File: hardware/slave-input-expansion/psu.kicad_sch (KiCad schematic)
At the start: 15 parts

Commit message: Diseño mecanico del ensamblaje
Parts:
- C4, C5: value (none) -> 100nF; footprint (none) -> Capacitor_SMD:C_1206_3216Metric_Pad1.33x1.80mm_HandSolder
- C6, C7: value (none) -> 470uF; footprint (none) -> libs:CAP_10x10_SMD_THT
- D2: value (none) -> LED; footprint (none) -> LED_SMD:LED_1206_3216Metric
- D3, D4: value (none) -> SS14; footprint (none) -> Diode_SMD:D_SMA_Handsoldering
- L1, L2: value (none) -> 68uH; footprint (none) -> libs:L_12x12mm_H8mm
- R25: value (none) -> 4K7; footprint (none) -> Resistor_SMD:R_1206_3216Metric
- R26: value (none) -> 5.6K; footprint (none) -> Resistor_THT:R_Axial_DIN0204_L3.6mm_D1.6mm_P2.54mm_Vertical
- R27: value (none) -> 12K; footprint (none) -> Resistor_THT:R_Axial_DIN0204_L3.6mm_D1.6mm_P2.54mm_Vertical
- U12, U13: value (none) -> LM2596S-3.3; footprint (none) -> libs:TO-263-5_TabPin3
- U14: value (none) -> AMS1117-5.0; footprint (none) -> Package_TO_SOT_SMD:SOT-223-3_TabPin2
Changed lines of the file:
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@@
     (in_bom yes) (on_board yes)
     (property "Reference" "U13" (id 0) (at 107.95 80.01 0))
-    (property "Value" "" (id 1) (at 120.65 80.01 0))
-    (property "Footprint" "" (id 2) (at 118.11 92.71 0)
+    (property "Value" "LM2596S-3.3" (id 1) (at 120.65 80.01 0))
+    (property "Footprint" "libs:TO-263-5_TabPin3" (id 2) (at 118.11 92.71 0)
       (effects (font (size 1.27 1.27) italic) (justify left) hide)
     )
@@
       (effects (font (size 1.27 1.27)) (justify right))
     )
-    (property "Value" "" (id 1) (at 57.6072 90.2208 90)
+    (property "Value" "LED" (id 1) (at 57.6072 90.2208 90)
       (effects (font (size 1.27 1.27)) (justify right))
     )
-    (property "Footprint" "" (id 2) (at 54.61 88.9 0)
+    (property "Footprint" "LED_SMD:LED_1206_3216Metric" (id 2) (at 54.61 88.9 0)
       (effects (font (size 1.27 1.27)) hide)
     )
@@
       (effects (font (size 1.27 1.27)) (justify left))
     )
-    (property "Value" "" (id 1) (at 56.388 100.203 0)
-      (effects (font (size 1.27 1.27)) (justify left))
-    )
-    (property "Footprint" "" (id 2) (at 52.832 99.06 90)
+    (property "Value" "4K7" (id 1) (at 56.388 100.203 0)
+      (effects (font (size 1.27 1.27)) (justify left))
+    )
+    (property "Footprint" "Resistor_SMD:R_1206_3216Metric" (id 2) (at 52.832 99.06 90)
       (effects (font (size 1.27 1.27)) hide)
     )
@@
       (effects (font (size 1.27 1.27)) (justify left))
     )
-    (property "Value" "" (id 1) (at 95.25 97.79 0)
-      (effects (font (size 1.27 1.27)) (justify left))
-    )
-    (property "Footprint" "" (id 2) (at 94.9452 99.06 0)
+    (property "Value" "100nF" (id 1) (at 95.25 97.79 0)
+      (effects (font (size 1.27 1.27)) (justify left))
+    )
+    (property "Footprint" "Capacitor_SMD:C_1206_3216Metric_Pad1.33x1.80mm_HandSolder" (id 2) (at 94.9452 99.06 0)
       (effects (font (size 1.27 1.27)) hide)
     )
@@
       (effects (font (size 1.27 1.27)) (justify left))
     )
-    (property "Value" "" (id 1) (at 134.112 96.393 90)
-      (effects (font (size 1.27 1.27)) (justify left))
-    )
-    (property "Footprint" "" (id 2) (at 127.635 95.25 0)
+    (property "Value" "SS14" (id 1) (at 134.112 96.393 90)
+      (effects (font (size 1.27 1.27)) (justify left))
+    )
+    (property "Footprint" "Diode_SMD:D_SMA_Handsoldering" (id 2) (at 127.635 95.25 0)
       (effects (font (size 1.27 1.27)) hide)
     )
@@
       (effects (font (size 1.27 1.27)) (justify left))
     )
-    (property "Value" "" (id 1) (at 182.0672 95.25 0)
-      (effects (font (size 1.27 1.27)) (justify left))
-    )
-    (property "Footprint" "" (id 2) (at 180.0352 99.06 0)
+    (property "Value" "470uF" (id 1) (at 182.0672 95.25 0)
+      (effects (font (size 1.27 1.27)) (justify left))
+    )
+    (property "Footprint" "libs:CAP_10x10_SMD_THT" (id 2) (at 180.0352 99.06 0)
       (effects (font (size 1.27 1.27)) hide)
     )
@@
     (in_bom yes) (on_board yes)
     (property "Reference" "L2" (id 0) (at 147.32 90.17 90))
-    (property "Value" "" (id 1) (at 152.4 90.17 90))
-    (property "Footprint" "" (id 2) (at 149.86 88.9 0)
+    (property "Value" "68uH" (id 1) (at 152.4 90.17 90))
+    (property "Footprint" "libs:L_12x12mm_H8mm" (id 2) (at 149.86 88.9 0)
       (effects (font (size 1.27 1.27)) hide)
     )
@@
     (in_bom yes) (on_board yes)
     (property "Reference" "U14" (id 0) (at 232.41 101.8032 0))
-    (property "Value" "" (id 1) (at 232.41 104.1146 0))
-    (property "Footprint" "" (id 2) (at 232.41 102.87 0)
+    (property "Value" "AMS1117-5.0" (id 1) (at 232.41 104.1146 0))
+    (property "Footprint" "Package_TO_SOT_SMD:SOT-223-3_TabPin2" (id 2) (at 232.41 102.87 0)
       (effects (font (size 1.27 1.27)) hide)
     )
@@
     (in_bom yes) (on_board yes)
     (property "Reference" "L1" (id 0) (at 147.32 53.34 90))
-    (property "Value" "" (id 1) (at 152.4 53.34 90))
-    (property "Footprint" "" (id 2) (at 149.86 52.07 0)
+    (property "Value" "68uH" (id 1) (at 152.4 53.34 90))
+    (property "Footprint" "libs:L_12x12mm_H8mm" (id 2) (at 149.86 52.07 0)
       (effects (font (size 1.27 1.27)) hide)
     )
@@
       (effects (font (size 1.27 1.27)) (justify left))
     )
-    (property "Value" "" (id 1) (at 134.112 59.563 90)
-      (effects (font (size 1.27 1.27)) (justify left))
-    )
-    (property "Footprint" "" (id 2) (at 127.635 58.42 0)
+    (property "Value" "SS14" (id 1) (at 134.112 59.563 90)
+      (effects (font (size 1.27 1.27)) (justify left))
+    )
+    (property "Footprint" "Diode_SMD:D_SMA_Handsoldering" (id 2) (at 127.635 58.42 0)
       (effects (font (size 1.27 1.27)) hide)
     )
@@
       (effects (font (size 1.27 1.27)) (justify left))
     )
-    (property "Value" "" (id 1) (at 182.0672 58.42 0)
-      (effects (font (size 1.27 1.27)) (justify left))
-    )
-    (property "Footprint" "" (id 2) (at 180.0352 62.23 0)
+    (property "Value" "470uF" (id 1) (at 182.0672 58.42 0)
+      (effects (font (size 1.27 1.27)) (justify left))
+    )
+    (property "Footprint" "libs:CAP_10x10_SMD_THT" (id 2) (at 180.0352 62.23 0)
       (effects (font (size 1.27 1.27)) hide)
     )
@@
     (in_bom yes) (on_board yes)
     (property "Reference" "R26" (id 0) (at 137.16 44.45 90))
-    (property "Value" "" (id 1) (at 138.43 49.53 90))
-    (property "Footprint" "" (id 2) (at 138.43 48.768 90)
+    (property "Value" "5.6K" (id 1) (at 138.43 49.53 90))
+    (property "Footprint" "Resistor_THT:R_Axial_DIN0204_L3.6mm_D1.6mm_P2.54mm_Vertical" (id 2) (at 138.43 48.768 90)
       (effects (font (size 1.27 1.27)) hide)
     )
@@
     (in_bom yes) (on_board yes)
     (property "Reference" "U12" (id 0) (at 107.95 43.18 0))
-    (property "Value" "" (id 1) (at 120.65 43.18 0))
-    (property "Footprint" "" (id 2) (at 118.11 55.88 0)
+    (property "Value" "LM2596S-3.3" (id 1) (at 120.65 43.18 0))
+    (property "Footprint" "libs:TO-263-5_TabPin3" (id 2) (at 118.11 55.88 0)
       (effects (font (size 1.27 1.27) italic) (justify left) hide)
     )
@@
     (in_bom yes) (on_board yes)
     (property "Reference" "R27" (id 0) (at 148.59 44.45 90))
-    (property "Value" "" (id 1) (at 149.86 49.53 90))
-    (property "Footprint" "" (id 2) (at 149.86 48.768 90)
+    (property "Value" "12K" (id 1) (at 149.86 49.53 90))
+    (property "Footprint" "Resistor_THT:R_Axial_DIN0204_L3.6mm_D1.6mm_P2.54mm_Vertical" (id 2) (at 149.86 48.768 90)
       (effects (font (size 1.27 1.27)) hide)
     )
@@
       (effects (font (size 1.27 1.27)) (justify left))
     )
-    (property "Value" "" (id 1) (at 95.25 60.96 0)
-      (effects (font (size 1.27 1.27)) (justify left))
-    )
-    (property "Footprint" "" (id 2) (at 94.9452 62.23 0)
-      (effects (font (size 1.27 1.27)) hide)
-    )
+    (property "Value" "100nF" (id 1) (at 95.25 60.96 0)
+      (effects (font (size 1.27 1.27)) (justify left))
+    )
+    (property "Footprint" "Capacitor_SMD:C_1206_3216Metric_Pad1.33x1.80mm_HandSolder" (id 2) (at 94.9452 62.23 0)
+      (effects (font (size 1.27 1.27)) hide)
+    )

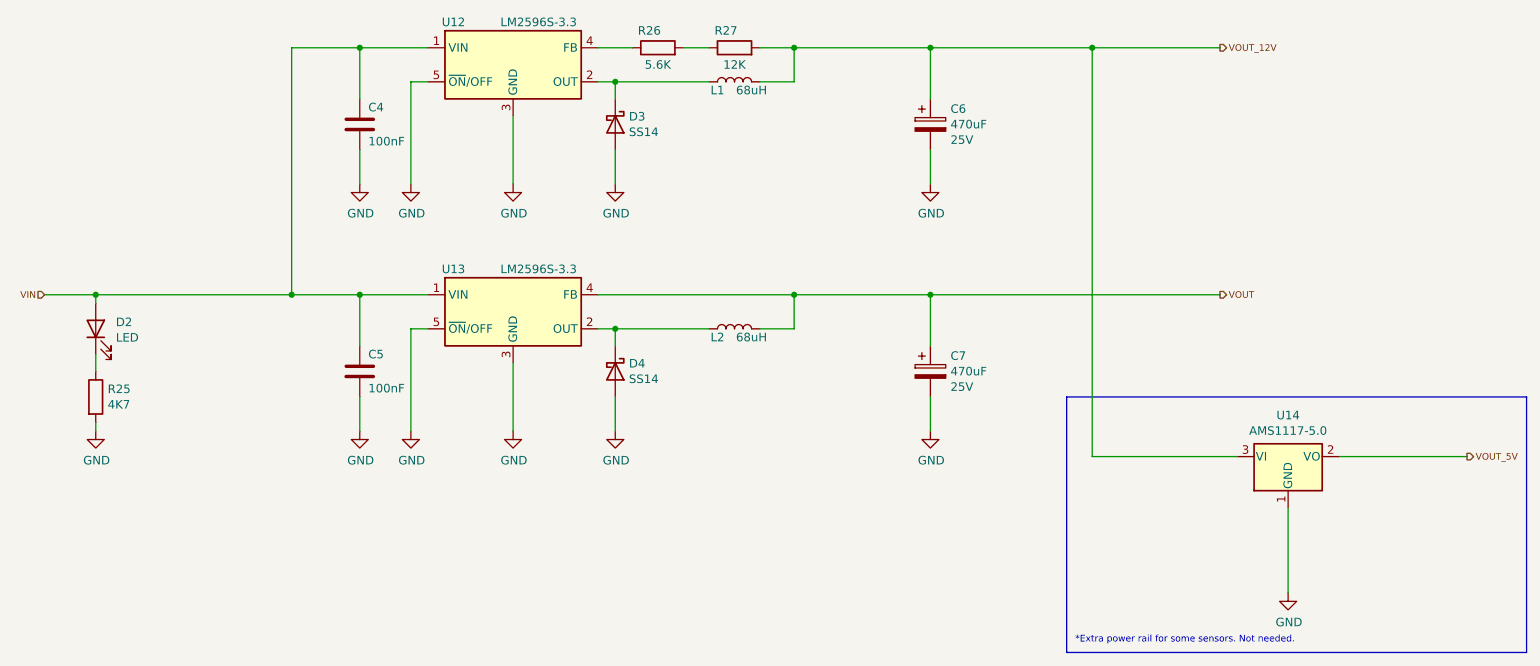
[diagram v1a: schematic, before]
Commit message: Routeo de la placa expansion
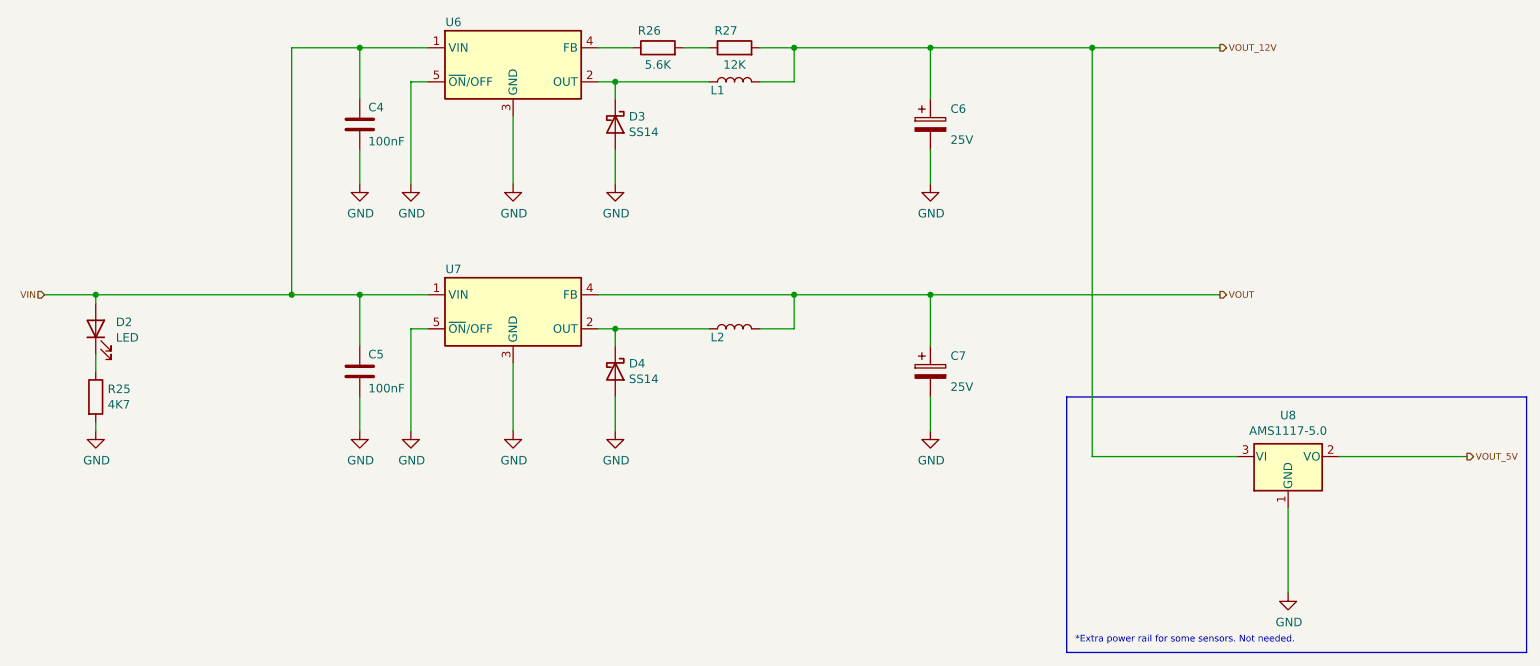
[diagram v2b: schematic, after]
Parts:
- C6, C7: value 470uF -> (none); footprint libs:CAP_10x10_SMD_THT -> (none)
- L1, L2: value 68uH -> (none); footprint libs:L_12x12mm_H8mm -> (none)
- U6: renamed from U12; value LM2596S-3.3 -> (none); footprint libs:TO-263-5_TabPin3 -> (none)
- U7: renamed from U13; value LM2596S-3.3 -> (none); footprint libs:TO-263-5_TabPin3 -> (none)
- renumbered U14 to U8
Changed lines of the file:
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@@
   (symbol (lib_id "Regulator_Switching:LM2596S-3.3") (at 116.84 86.36 0) (unit 1)
     (in_bom yes) (on_board yes)
-    (property "Reference" "U13" (id 0) (at 107.95 80.01 0))
-    (property "Value" "LM2596S-3.3" (id 1) (at 120.65 80.01 0))
-    (property "Footprint" "libs:TO-263-5_TabPin3" (id 2) (at 118.11 92.71 0)
+    (property "Reference" "U7" (id 0) (at 107.95 80.01 0))
+    (property "Value" "" (id 1) (at 120.65 80.01 0))
+    (property "Footprint" "" (id 2) (at 118.11 92.71 0)
       (effects (font (size 1.27 1.27) italic) (justify left) hide)
     )
@@
   (symbol (lib_id "power:GND") (at 54.61 104.14 0) (unit 1)
     (in_bom yes) (on_board yes)
-    (property "Reference" "#PWR040" (id 0) (at 54.61 110.49 0)
+    (property "Reference" "#PWR042" (id 0) (at 54.61 110.49 0)
       (effects (font (size 1.27 1.27)) hide)
     )
@@
   (symbol (lib_id "power:GND") (at 93.98 104.14 0) (unit 1)
     (in_bom yes) (on_board yes)
-    (property "Reference" "#PWR042" (id 0) (at 93.98 110.49 0)
+    (property "Reference" "#PWR044" (id 0) (at 93.98 110.49 0)
       (effects (font (size 1.27 1.27)) hide)
     )
@@
       (effects (font (size 1.27 1.27)) (justify left))
     )
-    (property "Value" "470uF" (id 1) (at 182.0672 95.25 0)
-      (effects (font (size 1.27 1.27)) (justify left))
-    )
-    (property "Footprint" "libs:CAP_10x10_SMD_THT" (id 2) (at 180.0352 99.06 0)
+    (property "Value" "" (id 1) (at 182.0672 95.25 0)
+      (effects (font (size 1.27 1.27)) (justify left))
+    )
+    (property "Footprint" "" (id 2) (at 180.0352 99.06 0)
       (effects (font (size 1.27 1.27)) hide)
     )
@@
   (symbol (lib_id "power:GND") (at 179.07 104.14 0) (unit 1)
     (in_bom yes) (on_board yes)
-    (property "Reference" "#PWR050" (id 0) (at 179.07 110.49 0)
+    (property "Reference" "#PWR052" (id 0) (at 179.07 110.49 0)
       (effects (font (size 1.27 1.27)) hide)
     )
@@
     (in_bom yes) (on_board yes)
     (property "Reference" "L2" (id 0) (at 147.32 90.17 90))
-    (property "Value" "68uH" (id 1) (at 152.4 90.17 90))
-    (property "Footprint" "libs:L_12x12mm_H8mm" (id 2) (at 149.86 88.9 0)
+    (property "Value" "" (id 1) (at 152.4 90.17 90))
+    (property "Footprint" "" (id 2) (at 149.86 88.9 0)
       (effects (font (size 1.27 1.27)) hide)
     )
@@
   (symbol (lib_id "power:GND") (at 116.84 104.14 0) (unit 1)
     (in_bom yes) (on_board yes)
-    (property "Reference" "#PWR046" (id 0) (at 116.84 110.49 0)
+    (property "Reference" "#PWR048" (id 0) (at 116.84 110.49 0)
       (effects (font (size 1.27 1.27)) hide)
     )
@@
   (symbol (lib_id "power:GND") (at 101.6 104.14 0) (unit 1)
     (in_bom yes) (on_board yes)
-    (property "Reference" "#PWR044" (id 0) (at 101.6 110.49 0)
+    (property "Reference" "#PWR046" (id 0) (at 101.6 110.49 0)
       (effects (font (size 1.27 1.27)) hide)
     )
@@
   (symbol (lib_id "power:GND") (at 132.08 104.14 0) (unit 1)
     (in_bom yes) (on_board yes)
-    (property "Reference" "#PWR048" (id 0) (at 132.08 110.49 0)
+    (property "Reference" "#PWR050" (id 0) (at 132.08 110.49 0)
       (effects (font (size 1.27 1.27)) hide)
     )
@@
   (symbol (lib_id "power:GND") (at 232.41 128.27 0) (unit 1)
     (in_bom yes) (on_board yes)
-    (property "Reference" "#PWR051" (id 0) (at 232.41 134.62 0)
+    (property "Reference" "#PWR053" (id 0) (at 232.41 134.62 0)
       (effects (font (size 1.27 1.27)) hide)
     )
@@
   (symbol (lib_id "Regulator_Linear:AMS1117-5.0") (at 232.41 107.95 0) (unit 1)
     (in_bom yes) (on_board yes)
-    (property "Reference" "U14" (id 0) (at 232.41 101.8032 0))
+    (property "Reference" "U8" (id 0) (at 232.41 101.8032 0))
     (property "Value" "AMS1117-5.0" (id 1) (at 232.41 104.1146 0))
     (property "Footprint" "Package_TO_SOT_SMD:SOT-223-3_TabPin2" (id 2) (at 232.41 102.87 0)
@@
   (symbol (lib_id "power:GND") (at 93.98 67.31 0) (unit 1)
     (in_bom yes) (on_board yes)
-    (property "Reference" "#PWR041" (id 0) (at 93.98 73.66 0)
+    (property "Reference" "#PWR043" (id 0) (at 93.98 73.66 0)
       (effects (font (size 1.27 1.27)) hide)
     )
@@
   (symbol (lib_id "power:GND") (at 132.08 67.31 0) (unit 1)
     (in_bom yes) (on_board yes)
-    (property "Reference" "#PWR047" (id 0) (at 132.08 73.66 0)
+    (property "Reference" "#PWR049" (id 0) (at 132.08 73.66 0)
       (effects (font (size 1.27 1.27)) hide)
     )
@@
     (in_bom yes) (on_board yes)
     (property "Reference" "L1" (id 0) (at 147.32 53.34 90))
-    (property "Value" "68uH" (id 1) (at 152.4 53.34 90))
-    (property "Footprint" "libs:L_12x12mm_H8mm" (id 2) (at 149.86 52.07 0)
+    (property "Value" "" (id 1) (at 152.4 53.34 90))
+    (property "Footprint" "" (id 2) (at 149.86 52.07 0)
       (effects (font (size 1.27 1.27)) hide)
     )
@@
       (effects (font (size 1.27 1.27)) (justify left))
     )
-    (property "Value" "470uF" (id 1) (at 182.0672 58.42 0)
-      (effects (font (size 1.27 1.27)) (justify left))
-    )
-    (property "Footprint" "libs:CAP_10x10_SMD_THT" (id 2) (at 180.0352 62.23 0)
+    (property "Value" "" (id 1) (at 182.0672 58.42 0)
+      (effects (font (size 1.27 1.27)) (justify left))
+    )
+    (property "Footprint" "" (id 2) (at 180.0352 62.23 0)
       (effects (font (size 1.27 1.27)) hide)
     )
@@
   (symbol (lib_id "power:GND") (at 101.6 67.31 0) (unit 1)
     (in_bom yes) (on_board yes)
-    (property "Reference" "#PWR043" (id 0) (at 101.6 73.66 0)
+    (property "Reference" "#PWR045" (id 0) (at 101.6 73.66 0)
       (effects (font (size 1.27 1.27)) hide)
     )
@@
   (symbol (lib_id "Regulator_Switching:LM2596S-3.3") (at 116.84 49.53 0) (unit 1)
     (in_bom yes) (on_board yes)
-    (property "Reference" "U12" (id 0) (at 107.95 43.18 0))
-    (property "Value" "LM2596S-3.3" (id 1) (at 120.65 43.18 0))
-    (property "Footprint" "libs:TO-263-5_TabPin3" (id 2) (at 118.11 55.88 0)
+    (property "Reference" "U6" (id 0) (at 107.95 43.18 0))
+    (property "Value" "" (id 1) (at 120.65 43.18 0))
+    (property "Footprint" "" (id 2) (at 118.11 55.88 0)
       (effects (font (size 1.27 1.27) italic) (justify left) hide)
     )
@@
   (symbol (lib_id "power:GND") (at 116.84 67.31 0) (unit 1)
     (in_bom yes) (on_board yes)
-    (property "Reference" "#PWR045" (id 0) (at 116.84 73.66 0)
+    (property "Reference" "#PWR047" (id 0) (at 116.84 73.66 0)
       (effects (font (size 1.27 1.27)) hide)
     )
@@
   (symbol (lib_id "power:GND") (at 179.07 67.31 0) (unit 1)
     (in_bom yes) (on_board yes)
-    (property "Reference" "#PWR049" (id 0) (at 179.07 73.66 0)
-      (effects (font (size 1.27 1.27)) hide)
-    )
+    (property "Reference" "#PWR051" (id 0) (at 179.07 73.66 0)
+      (effects (font (size 1.27 1.27)) hide)
+    )
